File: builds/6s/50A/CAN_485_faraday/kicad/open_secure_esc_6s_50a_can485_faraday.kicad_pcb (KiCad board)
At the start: 4 copper layers, 25.4 x 60.1 mm, 59 parts, among them J1 SolderPad_1x04_SMD_P2.54mm, J2 SolderPad_1x02_SMD_P2.54mm, J3 SolderPad_1x02_SMD_P2.54mm, J4A SolderWirePad_1x01_SMD_5x10mm, J4B SolderWirePad_1x01_SMD_5x10mm, J4C SolderWirePad_1x01_SMD_5x10mm, J5A SolderWire-6sqmm_1x01_D3.5mm_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, J5B SolderWire-6sqmm_1x01_D3.5mm_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, Q1 Toshiba_2-5W1A_SOP-Advance-N_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, Q2 Toshiba_2-5W1A_SOP-Advance-N_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, Q3 Toshiba_2-5W1A_SOP-Advance-N_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, Q4 Toshiba_2-5W1A_SOP-Advance-N_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, Q5 Toshiba_2-5W1A_SOP-Advance-N_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, Q6 Toshiba_2-5W1A_SOP-Advance-N_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, U1 LQFP-64_10x10mm_P0.5mm, U2 Infineon_PG-USON-10-2-4_3x3mm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, U3 SOIC-20W_7.5x12.8mm_P1.27mm, U4 SOIC-20W_7.5x12.8mm_P1.27mm, U5 TI_RTA0040B_WQFN-40_6x6mm_P0.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, U6 SOIC-8_3.9x4.9mm_P1.27mm, U7 SOIC-8_3.9x4.9mm_P1.27mm, U8 SOIC-8_3.9x4.9mm_P1.27mm

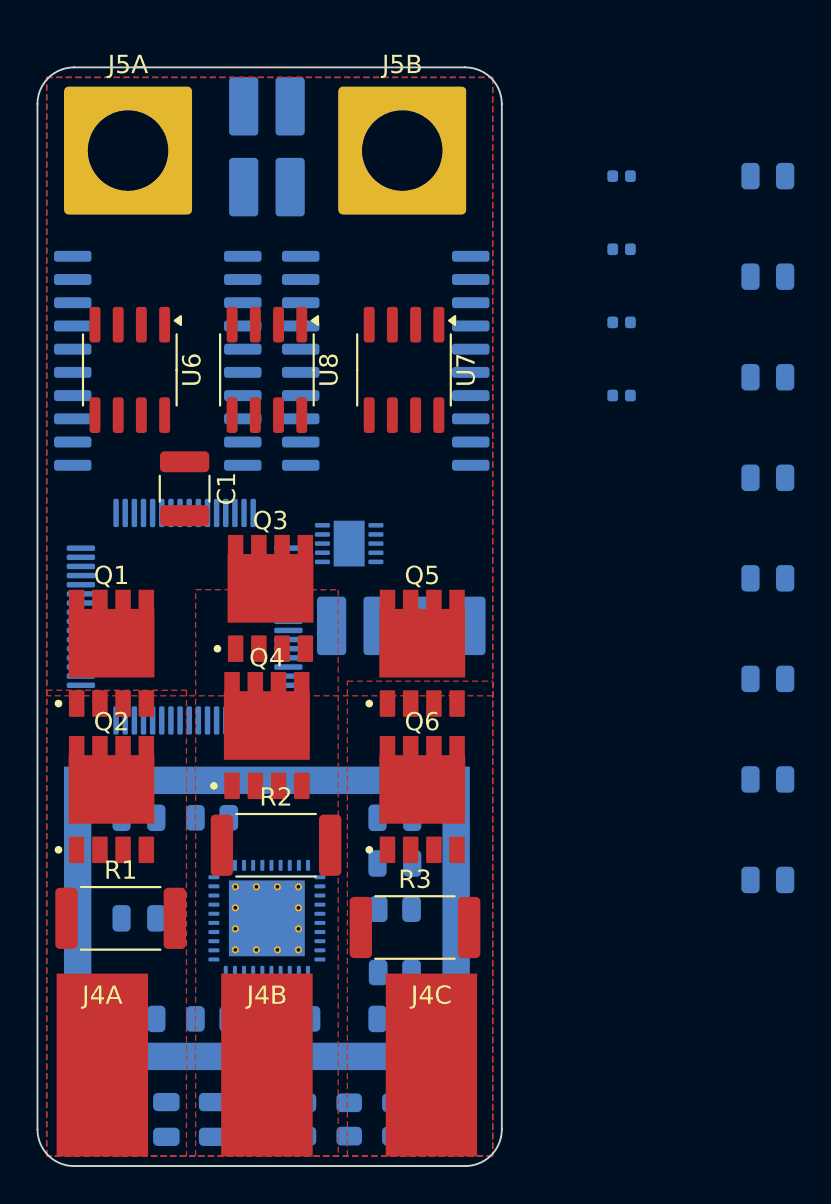
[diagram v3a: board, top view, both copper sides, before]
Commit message: Shrink J1 to a 1.27 mm probe pattern: 36.0 -> 12.0 mm2
J1 is the SWD debug port (SWDIO/SWCLK to U1.12/U1.13, plus 3V3 and GND). It
was using the same 2.54 mm wire-solder pads as J2/J3, which it does not need:
gen_smd_solder_pad_footprints.py already argued "For J1 (SWD) this is fine --
it is a bring-up/debug interface, not a flight connection."

    was  SolderPad_1x04_SMD_P2.54mm         9.22 x 3.20 mm, 36.0 mm2
    now  SolderPad_1x04_SMD_P1.27mm_Probe   4.71 x 1.80 mm, 12.0 mm2

1.27 mm is the pitch standard pogo-pin debug jigs use, so an off-the-shelf
4-pin inline fixture fits, and staying single-row keeps that fixture trivial.
A 2x2 grid would have saved a further ~2.5 mm2 but needs a custom one.
Pad-to-pad gap is 0.37 mm. Rejected: Tag-Connect TC2030, which looks like the
compact answer but needs three through-board alignment holes -- on a
double-sided board those cost their area twice, a net loss here.

The generator is now parameterised per variant rather than by module-level
constants, and carries a separate description template for probe pads so the
new footprint cannot be mistaken for a wire pad. J2/J3 deliberately KEEP the
2.54 mm variant: they leave the board in service and their solder area is
load-bearing in a way J1's is not (TODO.md 12.5.k). Verified that both
existing footprints regenerate byte-identical apart from uuids.

Footprint swapped in both the schematic and the PCB with all four nets
preserved. ERC 0 errors.

Not caused by this change, noted while checking: 2 copper_edge_clearance on
J5A/J5B against the board's rounded-corner arcs are present both before and
after, so they predate the swap.

Co-Authored-By: Claude Opus 5 <noreply@anthropic.com>
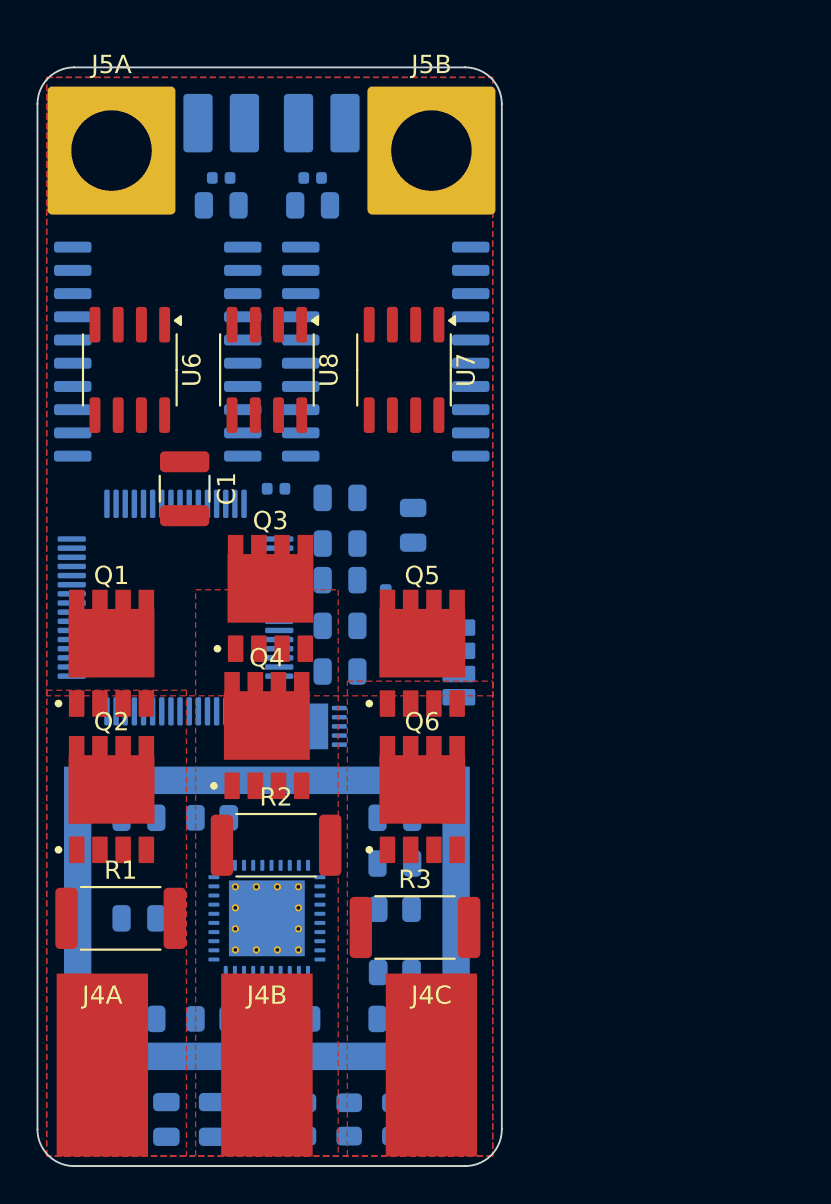
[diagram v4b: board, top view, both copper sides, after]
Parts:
- J1: value SolderPad_1x04_SMD_P2.54mm -> SolderPad_1x04_SMD_P1.27mm_Probe; footprint SolderPad_1x04_SMD_P2.54mm -> SolderPad_1x04_SMD_P1.27mm_Probe
- moved C16 35.9 mm to (35.0, 27.5), turned to 0 degrees
- moved C13 31.3 mm to (30.0, 27.5)
- moved C11 27.2 mm to (40.5, 45.0), turned to -90 degrees
- moved C12 26.3 mm to (36.5, 43.5)
- moved C18 26.0 mm to (36.5, 53.0)
- moved C17 24.9 mm to (36.5, 50.5)
- moved C14 24.1 mm to (36.5, 48.0)
- moved C15 23.5 mm to (36.5, 46.0)
- moved FB1 21.9 mm to (30.0, 26.0)
- moved FB3 19.9 mm to (39.0, 49.0), turned to -90 degrees
- moved FB4 19.6 mm to (33.0, 43.0)
- moved FB2 17.3 mm to (35.0, 26.0)
- moved U2 10.2 mm to (35.0, 56.0)
- moved J2 4.30 mm to (30.0, 23.0)
- moved J1 3.73 mm to (43.0, 52.5), turned to 90 degrees
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
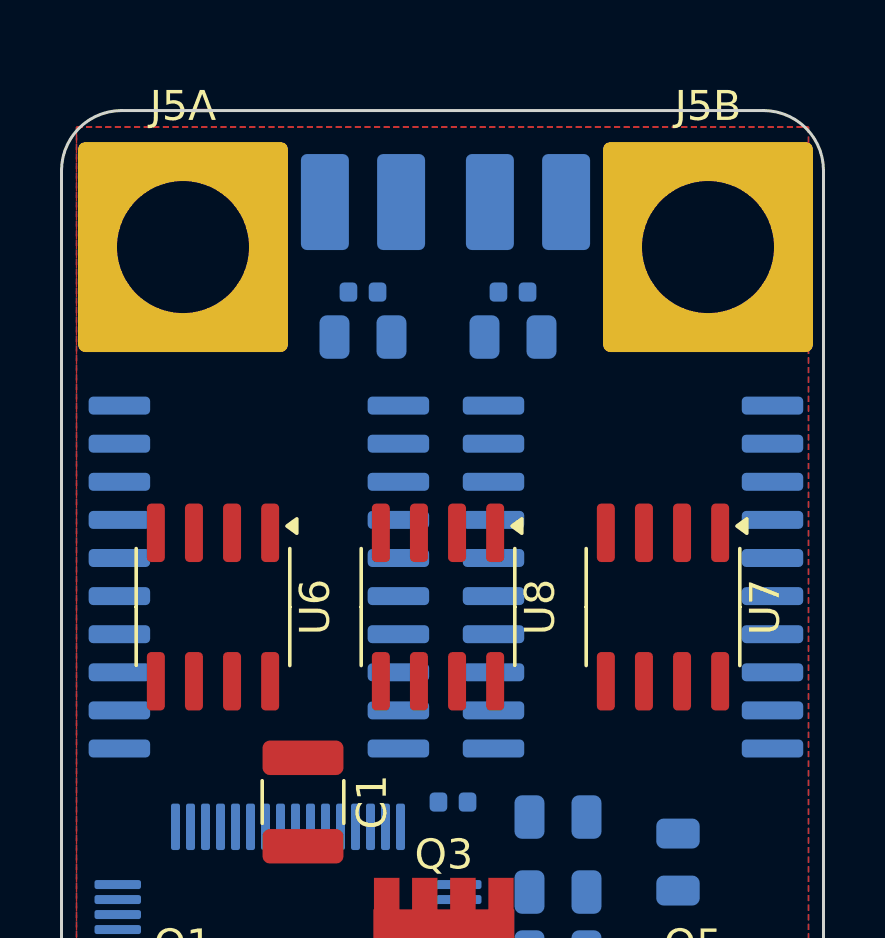
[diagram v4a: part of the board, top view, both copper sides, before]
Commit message: Write lock: use the MCU's internal seal, not a board-level fuse
Repo owner's call, and it is the right one. A fusible link on J1 would be
re-bridgeable by anyone who can solder -- tamper-evidence, not a seal. The
MSPM0G3507's own one-time configuration is the only irreversible option and
costs no board area. So J1 stays a plain 4-pad probe pattern; no fuse, no
solder bridge, no series element. No PCB change.

VERIFIED LOCALLY from [1] docs/datasheets/mspm0g3507.pdf:
  Sec 8.33 p.73  "Access to the device memory and configuration through the
                  BSL is protected by a 256-bit user-defined password, and it
                  is possible to completely disable the BSL in the device
                  configuration, if desired. The BSL is enabled by default
                  from TI."
  Sec 7          NONMAIN configuration NVM at 0x41C0.0000-0x41C0.0200 (512
                  bytes), separate from main flash -- where boot/debug
                  configuration lives.

NOT VERIFIED, AND THE PART THAT ACTUALLY MATTERS: the register-level debug
disable. [1] Sec 8.32 p.73 defers it completely -- "For a complete description
of the debug functionality offered on MSPM0 devices, see the debug chapter of
the technical reference manual." That manual is not in docs/datasheets/.

Added as REFERENCES.md [54], deliberately WITHOUT a document number: [1] names
the TRM only by title ("MSPM0 G-Series 80MHz Microcontrollers Technical
Reference Manual"), never by number, and guessing a SLAU number would be a
fabricated citation under AGENTS.md Sec 1.3.

Before the policy is implemented, [54] must answer: which NONMAIN field sets
the debug policy, whether the permanent state is genuinely one-way, how it
interacts with the 256-bit BSL password, and the production sequence. Sealing
before a verified image is unrecoverable, so the lock has to be the LAST
production step -- after the IDRIVE bench measurement (12.5.q) and any
firmware trim, or the board is bricked for tuning. Recorded 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
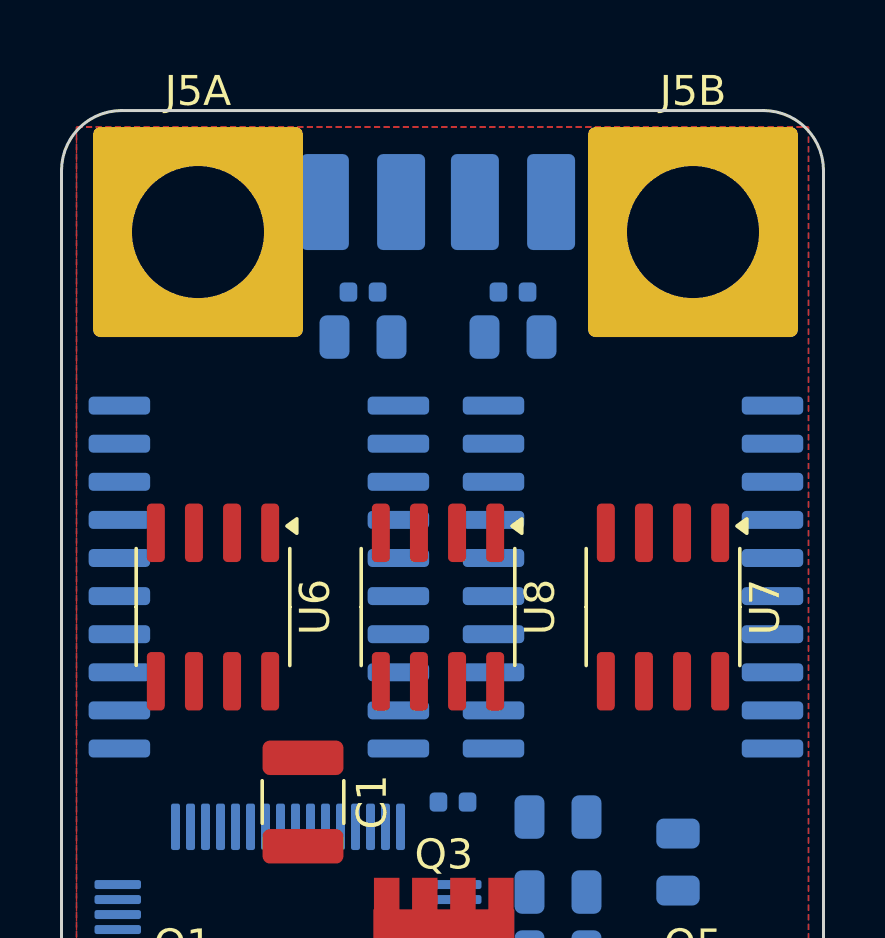
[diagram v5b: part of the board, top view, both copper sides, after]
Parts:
- moved J5A 0.71 mm to (24.5, 24.0)
- moved J5B 0.71 mm to (41.0, 24.0)
- moved J3 0.50 mm to (35.0, 23.0)
- turned U3 to 180 degrees
- turned U4 to 0 degrees

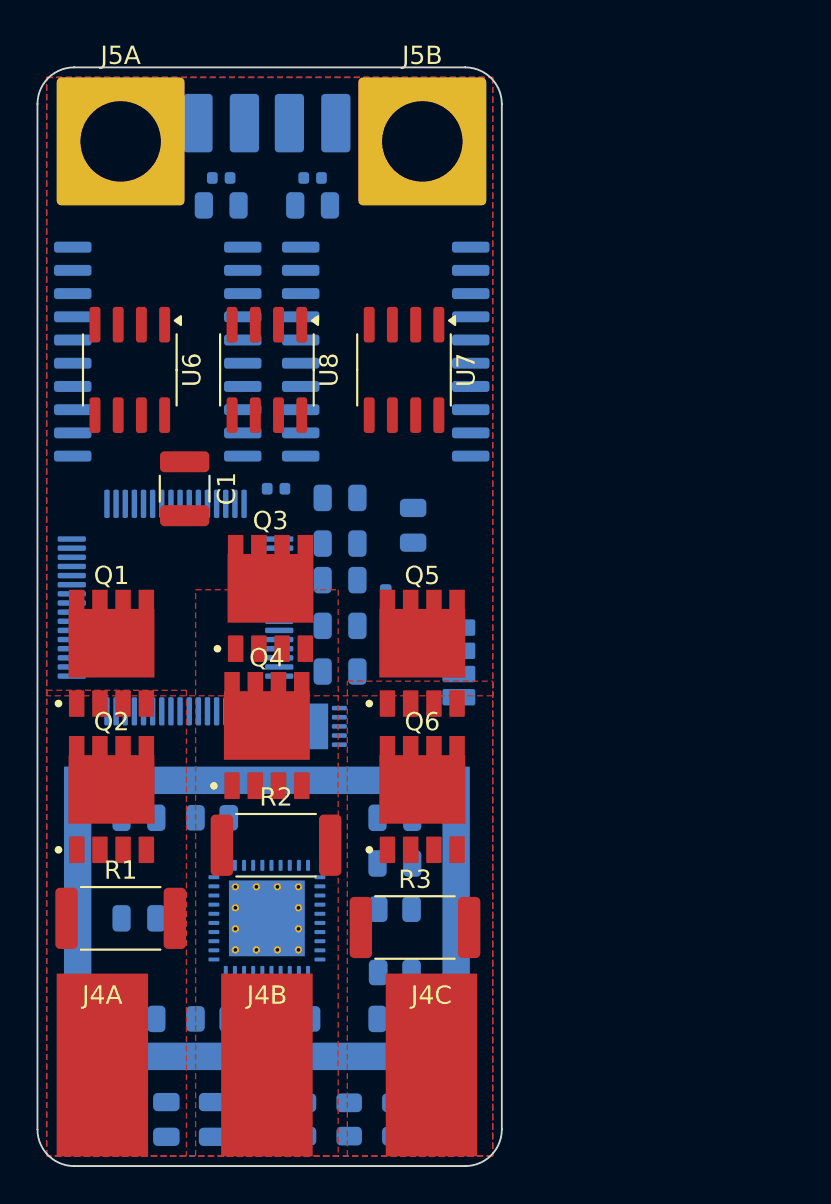
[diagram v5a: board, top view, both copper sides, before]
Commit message: Widen the board to 32 mm: U1's creepage goes 4.27 -> 9.50 mm
The repo owner chose width over length, and the numbers back it. Per
docs/tools/isolation_envelope.py, U1 (13.45 mm) cannot fit between two
isolated rows below 31.86 mm of board width; below that it must clear the
isolated section in Y instead, costing the creepage offset plus its own
height -- 19.07 mm of length for 6.46 mm of width, a 3x trade at essentially
constant area. The nacelle annulus accepts either width with 7-9 mm to spare,
so nothing mechanical forced the narrow option.

    board            25.40 -> 32.00 mm   (length unchanged, 60.10)
    U1 to isolated    4.27 ->  9.50 mm   (needs 7.5; 2.0 mm spare)

THE POWER STAGE DID NOT MOVE, AND DID NOT NEED TO. SH1 is a Wurth WE-SHC
3670209 [51] with a fixed 22.2 mm land that must sit directly under the FETs
for the shortest gate loop, so the FET columns are capped at the shield's
width however wide the board gets. Q1-Q6, SH1, U5, R1-R3 and J4A/B/C keep
their x; every added millimetre went to the isolated section and to U1.

A MISTAKE MADE AND REVERTED WITHIN THE SAME CHANGE: the first run moved J3
rightward along with U4, on the assumption that a connector follows its
transceiver. It does not here -- J5B, the pack GND terminal, already occupies
x 17.60..24.60, the space U4 vacates. J3 landed 1.20 mm from J5B.1, worse
than the 4.83 mm it started at. J3 was returned and the script now carries the
reason so the next reader does not repeat it.

STILL OPEN, AND WIDENING CANNOT FIX IT: the pack terminals and the isolated
comms share the top end.

    J2.1  <-> J5A.1   4.35 mm
    J3.2  <-> J5B.1   4.83 mm
    U3.20 <-> J5A.1   6.35 mm

J5A spans x 1.10..8.10 and J5B x 17.60..24.60, overlapping in x with where
both isolated groups must live, so they can separate only in Y. That is the
architecture question already referred to the owner in 12.5.ac -- pack to the
bottom, comms to the bottom, or accept the length.

U1's new centred position also overlaps J1 a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
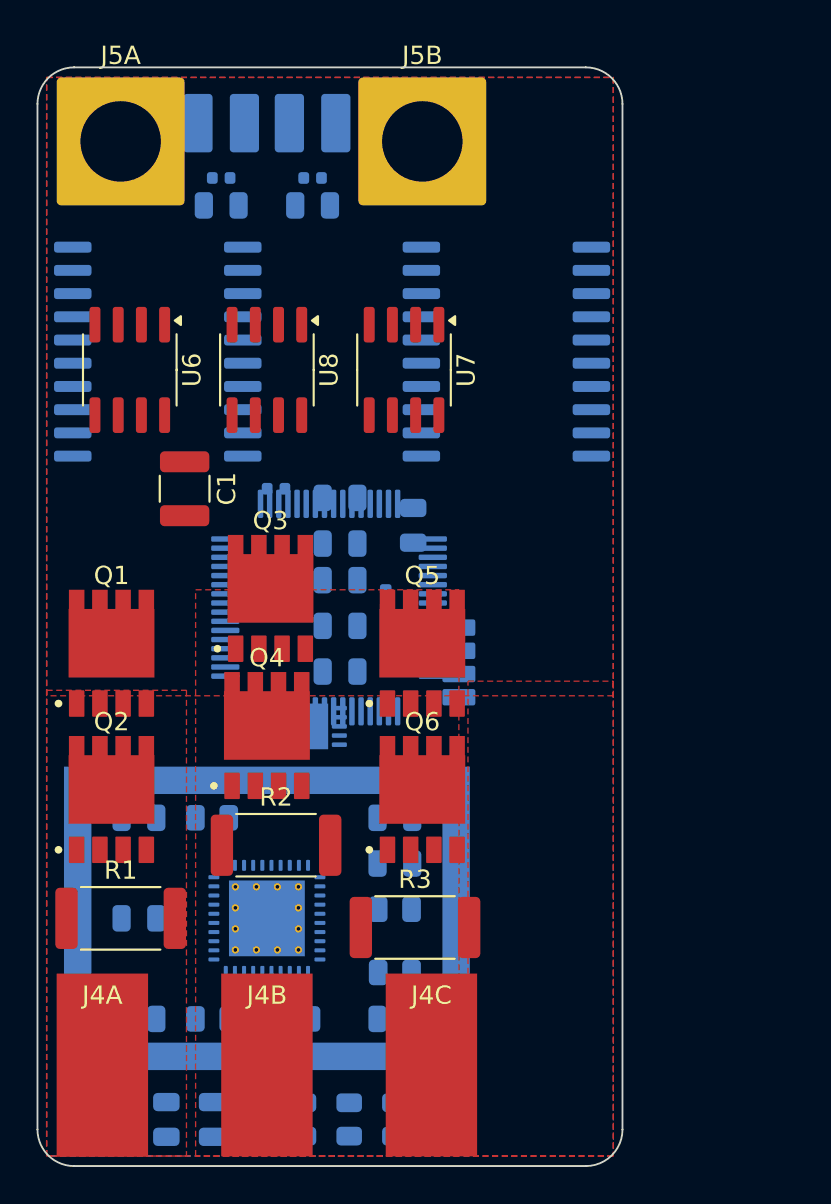
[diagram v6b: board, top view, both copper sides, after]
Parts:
- moved U1 8.40 mm to (35.9, 49.5)
- moved U4 6.60 mm to (45.6, 35.5)
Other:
- board size 25.4 x 60.1 mm -> 32 x 60.1 mm
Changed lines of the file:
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@@
 	(footprint "SOIC-20W_7.5x12.8mm_P1.27mm"
 		(layer "B.Cu")
-		(at 39 35.5)
+		(at 45.6 35.5)
 		(descr "SOIC, 20 Pin (JEDEC MS-013AC, https://www.analog.com/media/en/package-pcb-resources/package/233848rw_20.pdf), generated with kicad-footprint-generator ipc_gullwing_generator.py")
 		(tags "SOIC SO")
@@
 	(footprint "LQFP-64_10x10mm_P0.5mm"
 		(layer "B.Cu")
-		(at 27.5 49.5 180)
+		(at 35.899999 49.5 180)
 		(descr "LQFP, 64 Pin (https://www.analog.com/media/en/technical-documentation/data-sheets/ad7606_7606-6_7606-4.pdf), generated with kicad-footprint-generator ipc_gullwing_generator.py")
 		(tags "LQFP QFP")
@@
 	)
 	(gr_arc
-		(start 43.349999 19.95)
-		(mid 44.764213 20.535786)
-		(end 45.349999 21.95)
+		(start 49.949999 19.95)
+		(mid 51.364213 20.535786)
+		(end 51.949999 21.95)
 		(stroke
 			(width 0.1)
@@
 	)
 	(gr_arc
-		(start 45.349999 78.05)
-		(mid 44.764213 79.464214)
-		(end 43.349999 80.05)
+		(start 51.949999 78.05)
+		(mid 51.364213 79.464213)
+		(end 49.949999 80.05)
 		(stroke
 			(width 0.1)
@@
 	(gr_line
 		(start 21.95 19.95)
-		(end 43.349999 19.95)
+		(end 49.949999 19.95)
 		(stroke
 			(width 0.1)
@@
 	)
 	(gr_line
-		(start 43.349999 80.05)
+		(start 49.949999 80.05)
 		(end 21.95 80.05)
 		(stroke
@@
 	)
 	(gr_line
-		(start 45.349999 21.95)
-		(end 45.349999 78.05)
+		(start 51.949999 21.95)
+		(end 51.949999 78.05)
 		(stroke
 			(width 0.1)
@@
 		(polygon
 			(pts
-				(xy 28.6 48.525) (xy 36.4 48.525) (xy 36.4 79.5) (xy 28.6 79.5)
+				(xy 28.6 48.525) (xy 43 48.525) (xy 43 79.5) (xy 28.6 79.5)
 			)
 		)
@@
 		(polygon
 			(pts
-				(xy 36.9 53.525) (xy 44.85 53.525) (xy 44.85 79.5) (xy 36.9 79.5)
+				(xy 43.5 53.525) (xy 51.45 53.525) (xy 51.45 79.5) (xy 43.5 79.5)
 			)
 		)
@@
 		(polygon
 			(pts
-				(xy 20.45 20.5) (xy 44.85 20.5) (xy 44.85 54.325) (xy 20.45 54.325)
+				(xy 20.45 20.5) (xy 51.45 20.5) (xy 51.45 54.325) (xy 20.45 54.325)
 			)
 		)
@@
 		(polygon
 			(pts
-				(xy 20.45 20.5) (xy 44.849999 20.5) (xy 44.849999 79.5) (xy 20.45 79.5)
+				(xy 20.45 20.5) (xy 51.449999 20.5) (xy 51.449999 79.5) (xy 20.45 79.5)
 			)
 		)
@@
 		(polygon
 			(pts
-				(xy 20.75 70.5) (xy 44.55 70.5) (xy 44.55 79.2) (xy 20.75 79.2)
+				(xy 20.75 70.5) (xy 51.15 70.5) (xy 51.15 79.2) (xy 20.75 79.2)
 			)
 		)
@@
 		(polygon
 			(pts
-				(xy 20.45 20.5) (xy 44.849999 20.5) (xy 44.849999 79.5) (xy 20.45 79.5)
+				(xy 20.45 20.5) (xy 51.449999 20.5) (xy 51.449999 79.5) (xy 20.45 79.5)
 			)
 		)
@@
 		(polygon
 			(pts
-				(xy 20.45 20.5) (xy 44.849999 20.5) (xy 44.849999 54.5) (xy 20.45 54.5)
+				(xy 20.45 20.5) (xy 51.449999 20.5) (xy 51.449999 54.5) (xy 20.45 54.5)
 			)
 		)
@@
 		(polygon
 			(pts
-				(xy 20.45 54.5) (xy 44.849999 54.5) (xy 44.849999 79.5) (xy 20.45 79.5)
+				(xy 20.45 54.5) (xy 51.449999 54.5) (xy 51.449999 79.5) (xy 20.45 79.5)
 			)
 		)
